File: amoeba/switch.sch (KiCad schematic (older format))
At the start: 3 parts

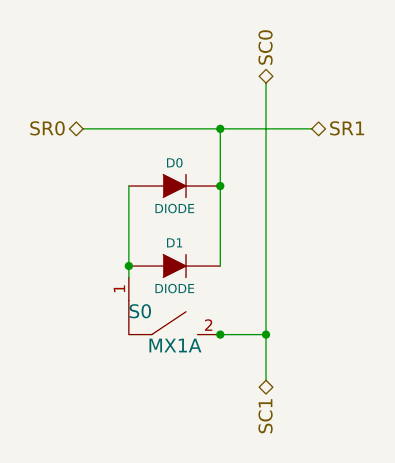
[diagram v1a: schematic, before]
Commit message: Adding net names to amoeba.
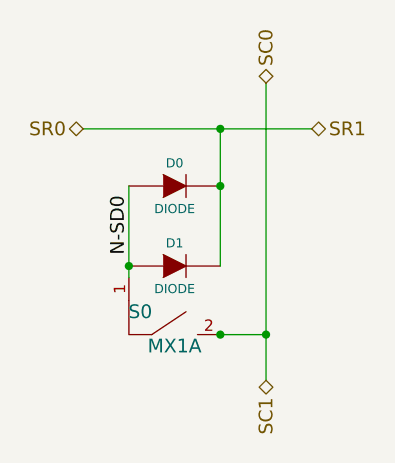
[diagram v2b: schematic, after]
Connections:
- net N-SD0: now reaches D0.1 (A), D1.1 (A), S0.1
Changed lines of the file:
@@
 Sheet 4 4
 Title ""
-Date "13 sep 2015"
+Date "15 sep 2015"
 Rev ""
 Comp ""
@@
 Connection ~ 5600 3850
 Connection ~ 5400 3850
+Text Label 5000 3500 1    60   ~ 0
+N-SD0
 $EndSCHEMATC
